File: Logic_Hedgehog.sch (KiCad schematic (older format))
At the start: 68 parts, among them J40 RaspberryPi3, J41 UART_EXT_1, J42 I2C_EXT_0, J43 I2C_EXT_0_EXP, J44 I2C_EXT_1, J45 SPI_EXT_0_0, J46 SPI_EXT_0_1, J47 SPI_EXT_1, J48 I/O_0-7, J49 I/O_8-15, J50 I/O_0-7, J51 I/O_8-15, J52 SERVO, J53 SERVO, J54 MOTORS, J55 MOTORS, U40 STM32F401VBT6, U41 74LVC2G32, U42 MC74VHC1G126, U43 IMU_ICM-20689, U44 DRV8835, U45 DRV8835, U46 Buzzer, Y40 Crystal

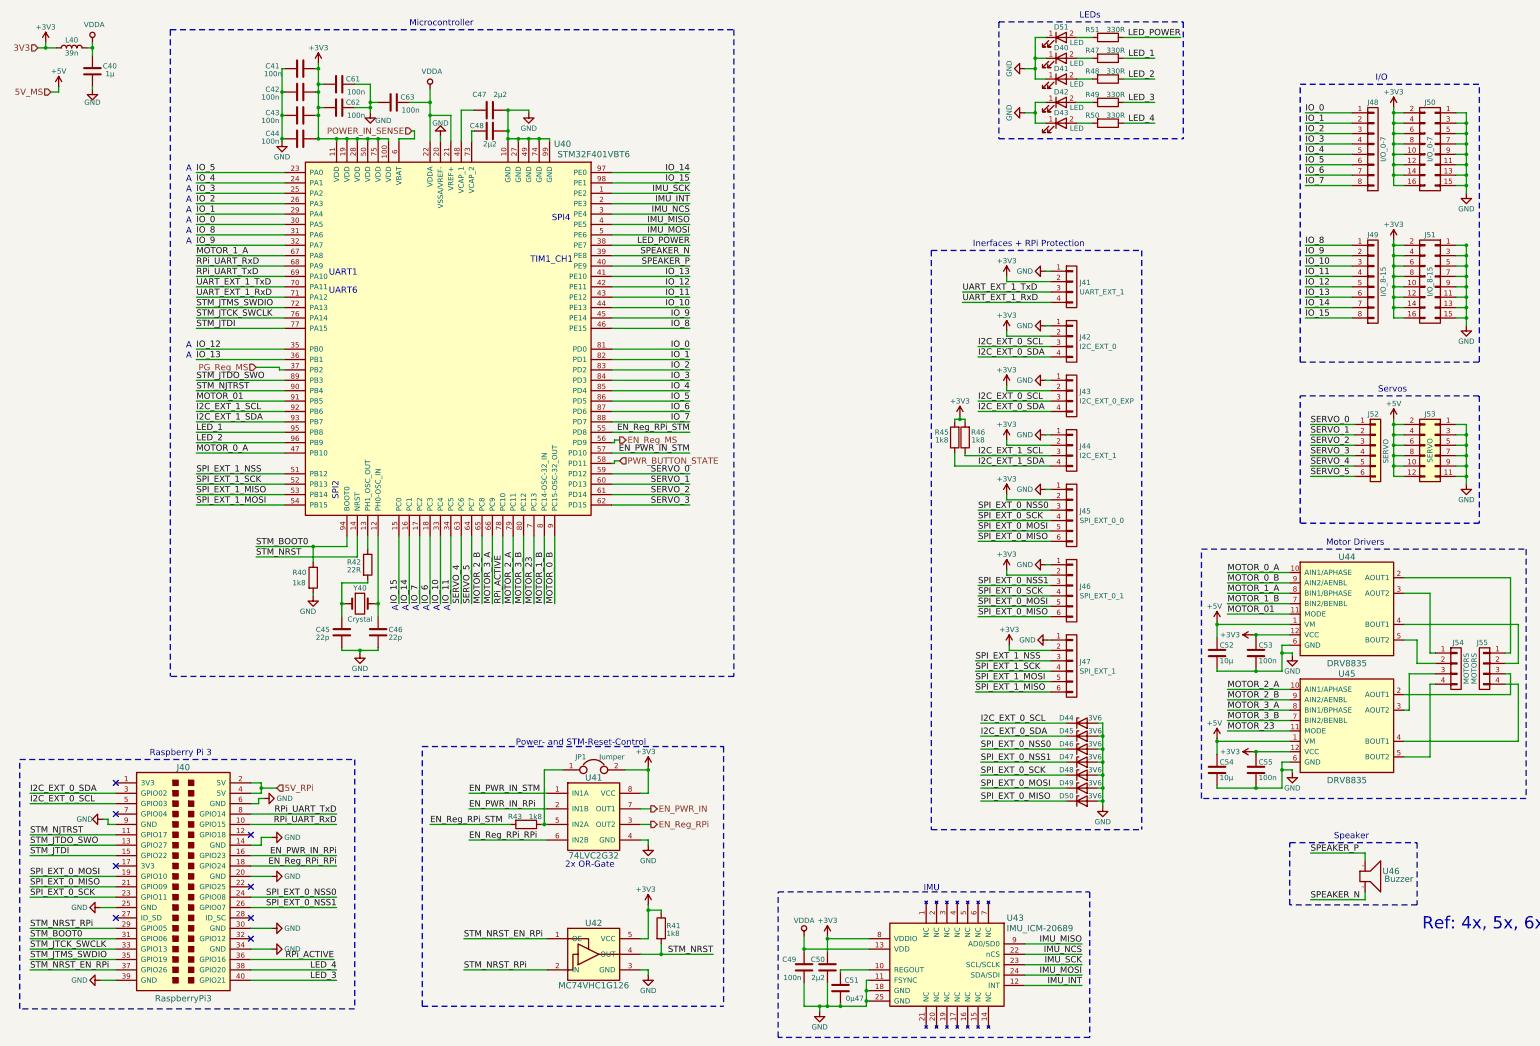
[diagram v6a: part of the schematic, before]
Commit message: component values changed documentation added
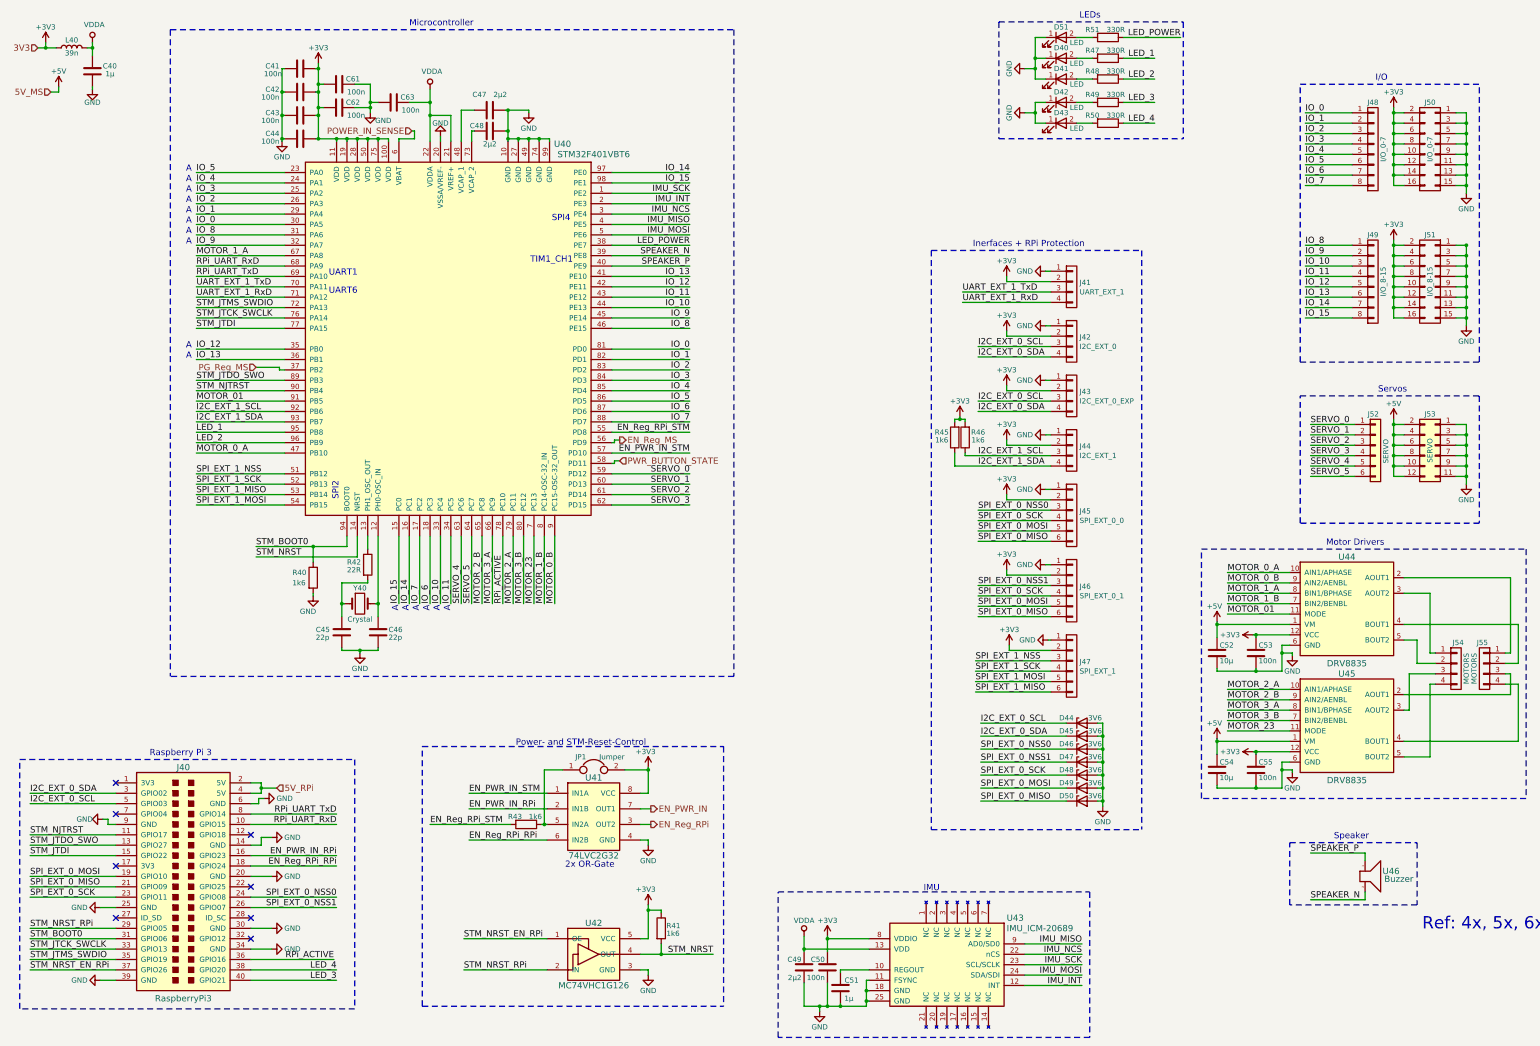
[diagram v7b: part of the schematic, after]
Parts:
- C49: value 100n -> 2µ2
- C50: value 2µ2 -> 100n
- C51: value 0µ47 -> 1µ
- R40, R41, R43, R45, R46: value 1k8 -> 1k6

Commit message: fixed library dependences, swapped inner layers
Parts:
- J41, J42, J43, J44, J54, J55: symbol CONN_01X04 -> Conn_01x04
- J45, J46, J47: symbol CONN_01X06 -> Conn_01x06
- J48, J49: symbol CONN_01X08 -> Conn_01x08
- J50, J51: symbol CONN_02X08 -> Conn_02x08_Odd_Even
